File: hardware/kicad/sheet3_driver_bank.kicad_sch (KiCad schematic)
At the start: 0 parts

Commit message: feat: populate all 4 KiCad schematic sheets with embedded symbols and wiring
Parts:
- added U101, U102, U103, U104, U105, U106, U107, U108, U109, U110, U111, U112, U113, U114, U115, U116, U117, U118, U119, U120, U121, U122, U123, U124, U125, U126, U127, U128, U129, U130, U131, U132: TC4427ACOA, symbol HPVE:TC4427A
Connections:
- new net +12V: U101.6 (VDD), U102.6 (VDD), U103.6 (VDD), U104.6 (VDD), U105.6 (VDD), U106.6 (VDD), U107.6 (VDD), U108.6 (VDD), U109.6 (VDD), U110.6 (VDD), U111.6 (VDD), U112.6 (VDD), U113.6 (VDD), U114.6 (VDD), U115.6 (VDD), U116.6 (VDD), U117.6 (VDD), U118.6 (VDD), U119.6 (VDD), U120.6 (VDD), U121.6 (VDD), U122.6 (VDD), U123.6 (VDD), U124.6 (VDD), U125.6 (VDD), U126.6 (VDD), U127.6 (VDD), U128.6 (VDD), U129.6 (VDD), U130.6 (VDD), U131.6 (VDD), U132.6 (VDD)
- new net DRV_1: U101.5 (OUTB)
- new net DRV_10: U105.7 (OUTA)
- new net DRV_11: U106.5 (OUTB)
- new net DRV_12: U106.7 (OUTA)
- new net DRV_13: U107.5 (OUTB)
- new net DRV_14: U107.7 (OUTA)
- new net DRV_15: U108.5 (OUTB)
- new net DRV_16: U108.7 (OUTA)
- new net DRV_17: U109.5 (OUTB)
- new net DRV_18: U109.7 (OUTA)
- new net DRV_19: U110.5 (OUTB)
- new net DRV_2: U101.7 (OUTA)
- new net DRV_20: U110.7 (OUTA)
- new net DRV_21: U111.5 (OUTB)
- new net DRV_22: U111.7 (OUTA)
- new net DRV_23: U112.5 (OUTB)
- new net DRV_24: U112.7 (OUTA)
- new net DRV_25: U113.5 (OUTB)
- new net DRV_26: U113.7 (OUTA)
- new net DRV_27: U114.5 (OUTB)
- new net DRV_28: U114.7 (OUTA)
- new net DRV_29: U115.5 (OUTB)
- new net DRV_3: U102.5 (OUTB)
- new net DRV_30: U115.7 (OUTA)
- new net DRV_31: U116.5 (OUTB)
- new net DRV_32: U116.7 (OUTA)
- new net DRV_33: U117.5 (OUTB)
- new net DRV_34: U117.7 (OUTA)
- new net DRV_35: U118.5 (OUTB)
- new net DRV_36: U118.7 (OUTA)
- new net DRV_37: U119.5 (OUTB)
- new net DRV_38: U119.7 (OUTA)
- new net DRV_39: U120.5 (OUTB)
- new net DRV_4: U102.7 (OUTA)
- new net DRV_40: U120.7 (OUTA)
- new net DRV_41: U121.5 (OUTB)
- new net DRV_42: U121.7 (OUTA)
- new net DRV_43: U122.5 (OUTB)
- new net DRV_44: U122.7 (OUTA)
- new net DRV_45: U123.5 (OUTB)
- new net DRV_46: U123.7 (OUTA)
- new net DRV_47: U124.5 (OUTB)
- new net DRV_48: U124.7 (OUTA)
- new net DRV_49: U125.5 (OUTB)
- new net DRV_5: U103.5 (OUTB)
- new net DRV_50: U125.7 (OUTA)
- new net DRV_51: U126.5 (OUTB)
- new net DRV_52: U126.7 (OUTA)
- new net DRV_53: U127.5 (OUTB)
- new net DRV_54: U127.7 (OUTA)
- new net DRV_55: U128.5 (OUTB)
- new net DRV_56: U128.7 (OUTA)
- new net DRV_57: U129.5 (OUTB)
- new net DRV_58: U129.7 (OUTA)
- new net DRV_59: U130.5 (OUTB)
- new net DRV_6: U103.7 (OUTA)
- new net DRV_60: U130.7 (OUTA)
- new net DRV_61: U131.5 (OUTB)
- new net DRV_62: U131.7 (OUTA)
- new net DRV_63: U132.5 (OUTB)
- new net DRV_64: U132.7 (OUTA)
- new net DRV_7: U104.5 (OUTB)
- new net DRV_8: U104.7 (OUTA)
- new net DRV_9: U105.5 (OUTB)
- new net GND: U101.3 (GND), U102.3 (GND), U103.3 (GND), U104.3 (GND), U105.3 (GND), U106.3 (GND), U107.3 (GND), U108.3 (GND), U109.3 (GND), U110.3 (GND), U111.3 (GND), U112.3 (GND), U113.3 (GND), U114.3 (GND), U115.3 (GND), U116.3 (GND), U117.3 (GND), U118.3 (GND), U119.3 (GND), U120.3 (GND), U121.3 (GND), U122.3 (GND), U123.3 (GND), U124.3 (GND), U125.3 (GND), U126.3 (GND), U127.3 (GND), U128.3 (GND), U129.3 (GND), U130.3 (GND), U131.3 (GND), U132.3 (GND)
- new net SIG_1: U101.4 (INB)
- new net SIG_10: U105.2 (INA)
- new net SIG_11: U106.4 (INB)
- new net SIG_12: U106.2 (INA)
- new net SIG_13: U107.4 (INB)
- new net SIG_14: U107.2 (INA)
- new net SIG_15: U108.4 (INB)
- new net SIG_16: U108.2 (INA)
- new net SIG_17: U109.4 (INB)
- new net SIG_18: U109.2 (INA)
- new net SIG_19: U110.4 (INB)
- new net SIG_2: U101.2 (INA)
- new net SIG_20: U110.2 (INA)
- new net SIG_21: U111.4 (INB)
- new net SIG_22: U111.2 (INA)
- new net SIG_23: U112.4 (INB)
- new net SIG_24: U112.2 (INA)
- new net SIG_25: U113.4 (INB)
- new net SIG_26: U113.2 (INA)
- new net SIG_27: U114.4 (INB)
- new net SIG_28: U114.2 (INA)
- new net SIG_29: U115.4 (INB)
- new net SIG_3: U102.4 (INB)
- new net SIG_30: U115.2 (INA)
- new net SIG_31: U116.4 (INB)
- new net SIG_32: U116.2 (INA)
- new net SIG_33: U117.4 (INB)
- new net SIG_34: U117.2 (INA)
- new net SIG_35: U118.4 (INB)
- new net SIG_36: U118.2 (INA)
- new net SIG_37: U119.4 (INB)
- new net SIG_38: U119.2 (INA)
- new net SIG_39: U120.4 (INB)
- new net SIG_4: U102.2 (INA)
- new net SIG_40: U120.2 (INA)
- new net SIG_41: U121.4 (INB)
- new net SIG_42: U121.2 (INA)
- new net SIG_43: U122.4 (INB)
- new net SIG_44: U122.2 (INA)
- new net SIG_45: U123.4 (INB)
- new net SIG_46: U123.2 (INA)
- new net SIG_47: U124.4 (INB)
- new net SIG_48: U124.2 (INA)
- new net SIG_49: U125.4 (INB)
- new net SIG_5: U103.4 (INB)
- new net SIG_50: U125.2 (INA)
- new net SIG_51: U126.4 (INB)
- new net SIG_52: U126.2 (INA)
- new net SIG_53: U127.4 (INB)
- new net SIG_54: U127.2 (INA)
- new net SIG_55: U128.4 (INB)
- new net SIG_56: U128.2 (INA)
- new net SIG_57: U129.4 (INB)
- new net SIG_58: U129.2 (INA)
- new net SIG_59: U130.4 (INB)
- new net SIG_6: U103.2 (INA)
- new net SIG_60: U130.2 (INA)
- new net SIG_61: U131.4 (INB)
- new net SIG_62: U131.2 (INA)
- new net SIG_63: U132.4 (INB)
- new net SIG_64: U132.2 (INA)
- new net SIG_7: U104.4 (INB)
- new net SIG_8: U104.2 (INA)
- new net SIG_9: U105.4 (INB)
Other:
- title: Sheet 3: TC4427 Driver Bank & 12V Power Bus -> Sheet 3: TC4427 Dual High-Speed Driver Bank (32 ICs / 64 Channels)

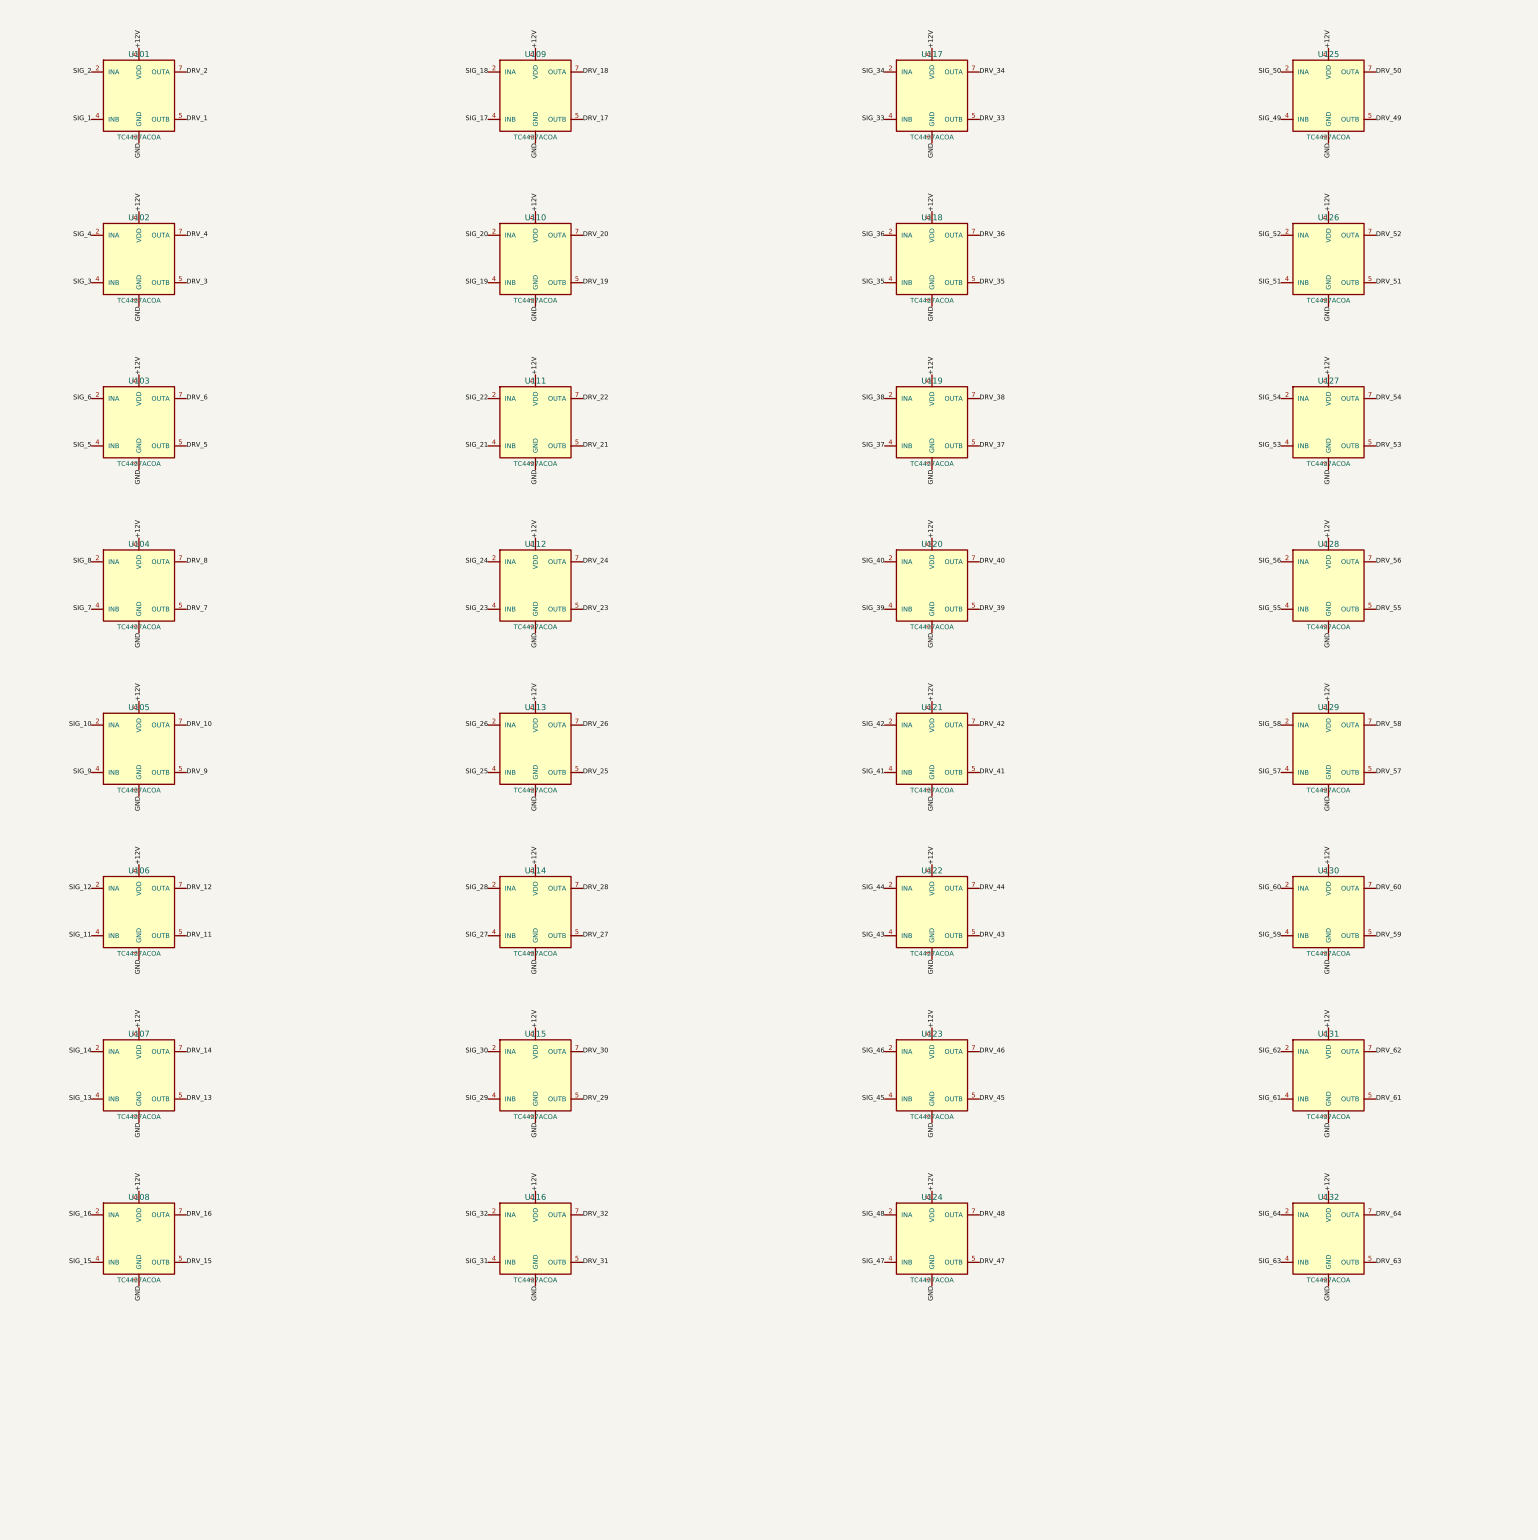
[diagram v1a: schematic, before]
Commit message: fix(kicad): assign valid footprints to all 105 symbols and add visible wiring
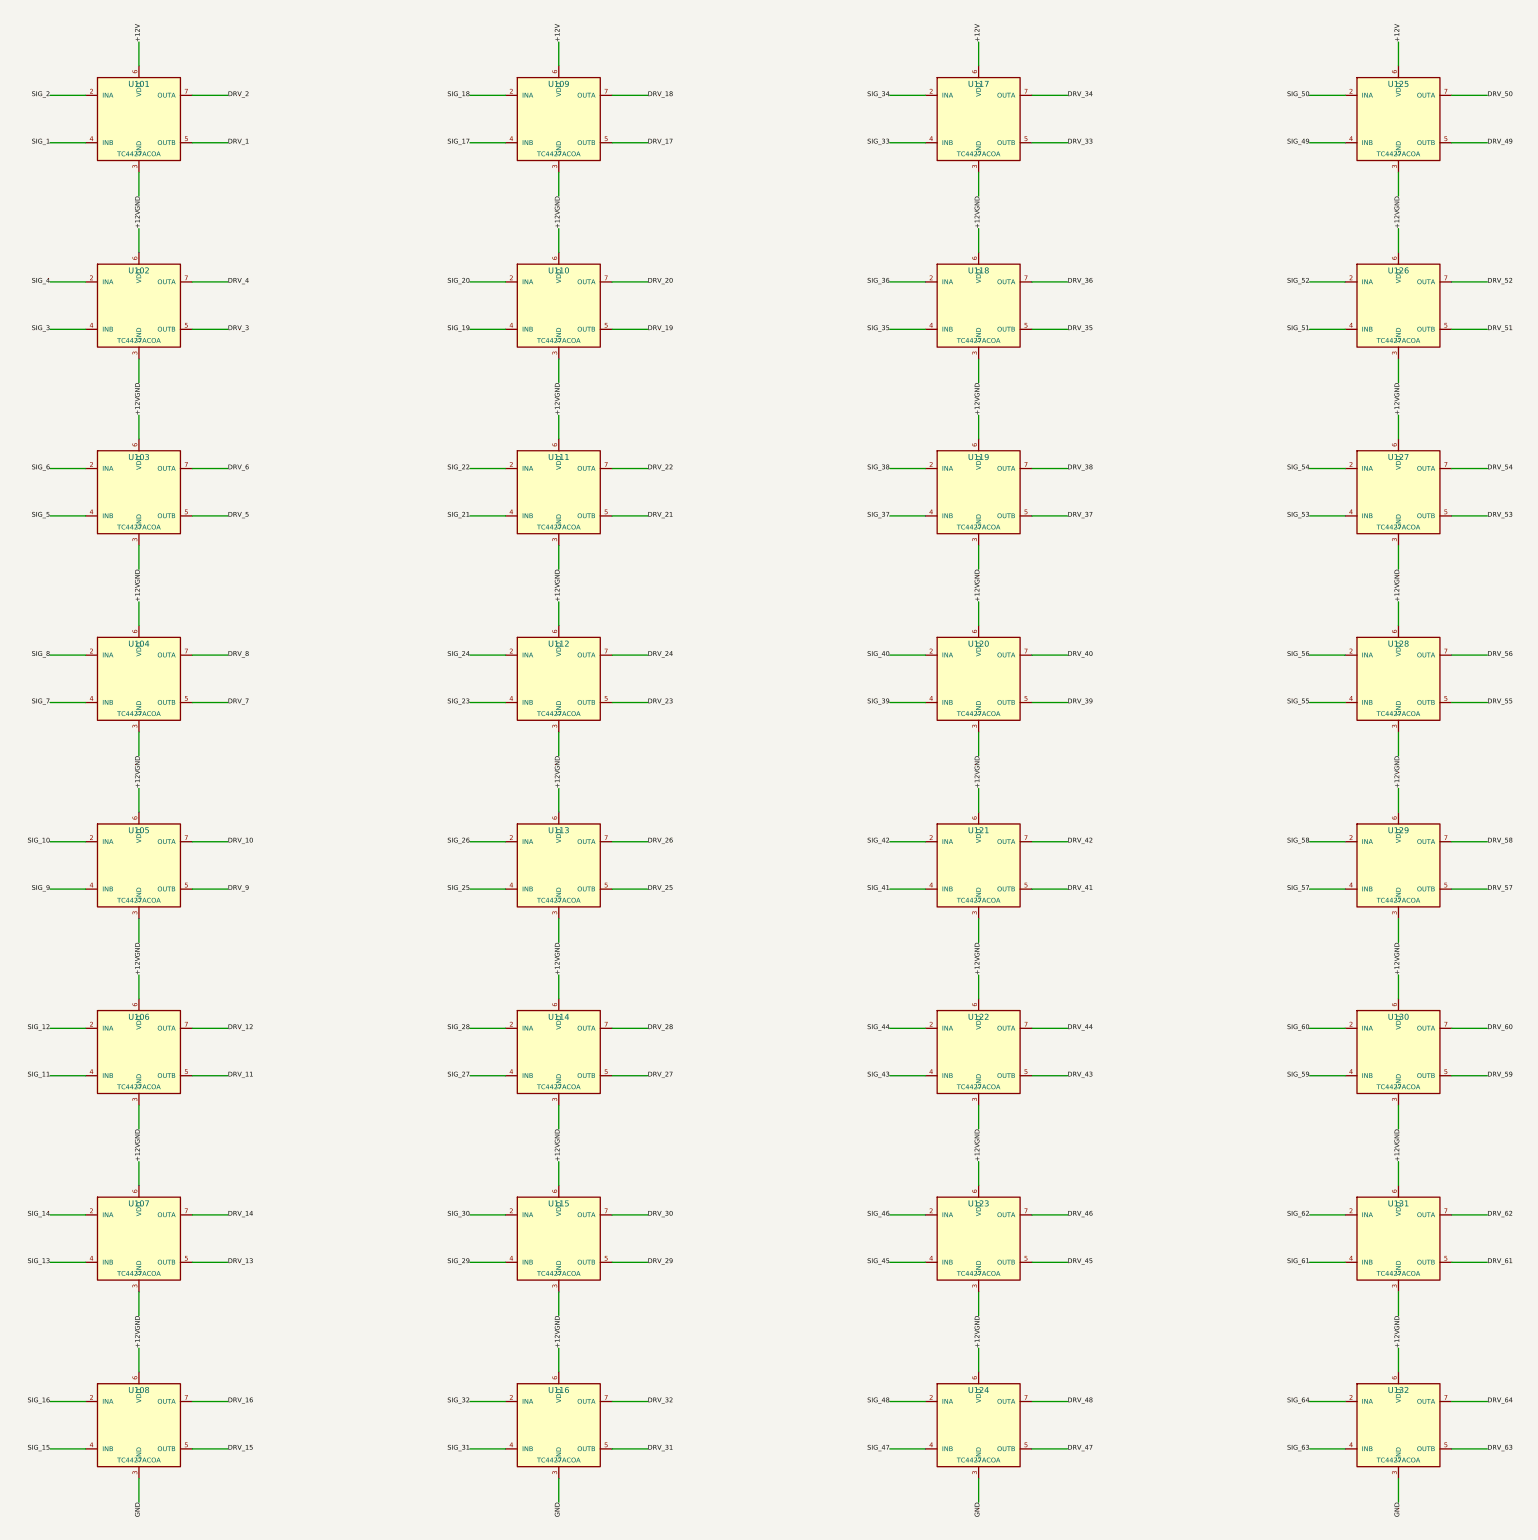
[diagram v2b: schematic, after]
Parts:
- U101, U102, U103, U104, U105, U106, U107, U108, U109, U110, U111, U112, U113, U114, U115, U116, U117, U118, U119, U120, U121, U122, U123, U124, U125, U126, U127, U128, U129, U130, U131, U132: footprint (none) -> Package_SO:SOIC-8_3.9x4.9mm_P1.27mm
